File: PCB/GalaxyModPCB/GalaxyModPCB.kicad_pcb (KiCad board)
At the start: 2 copper layers, 63.5 x 38.2 mm, 65 parts, among them J1 LED RGBW Connector, J2 USB to UART, J3 Motor Connector, J4 Projector Connector, J5 Debug Header, J6 Power Header, J7 Boot mode, Q1 IRLML0030, Q2 IRLML0030, Q3 IRLML0030, Q4 IRLML0030, Q5 IRLML0030, Q6 IRLML0030, SW1 On/Off, SW2 Colour, SW3 Brightness, SW4 Motor, U1 ESP32-WROOM-32, U2 AMS1117-3.3

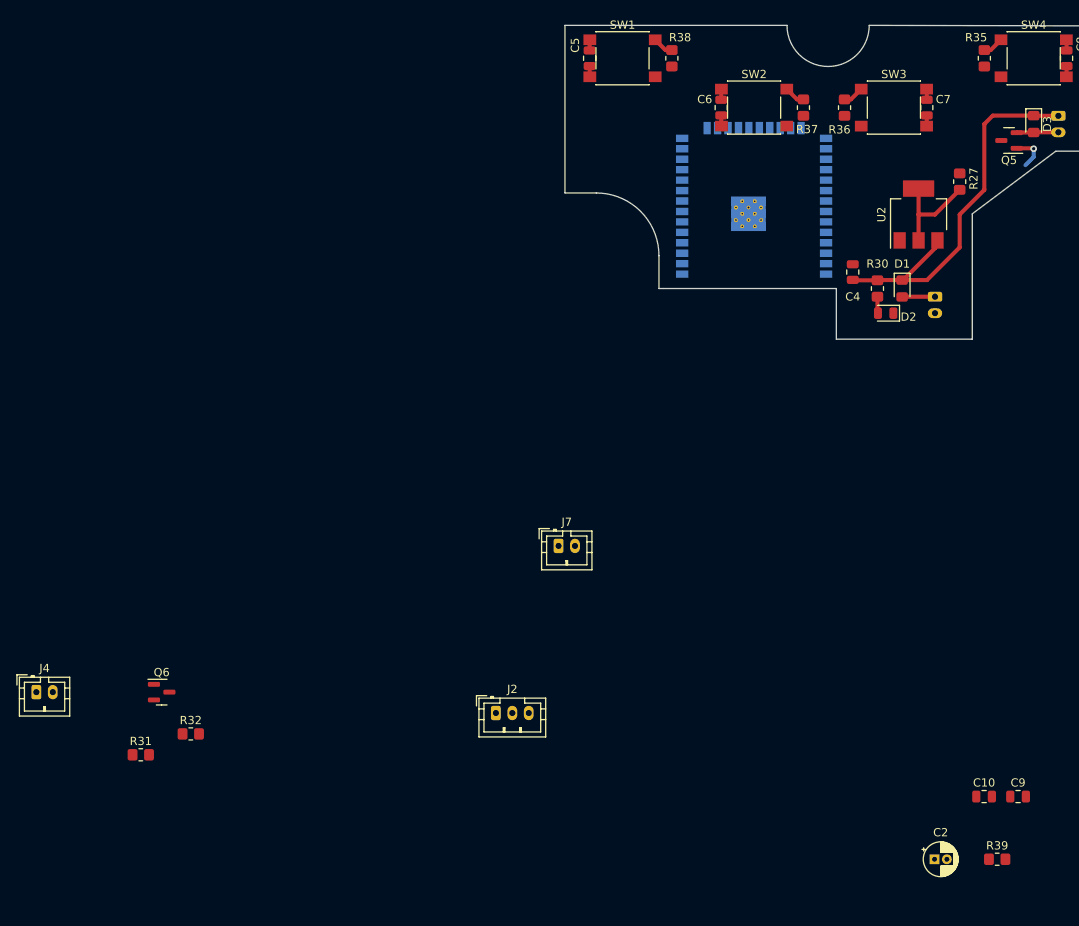
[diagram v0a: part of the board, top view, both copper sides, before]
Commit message: Connected power to esp32
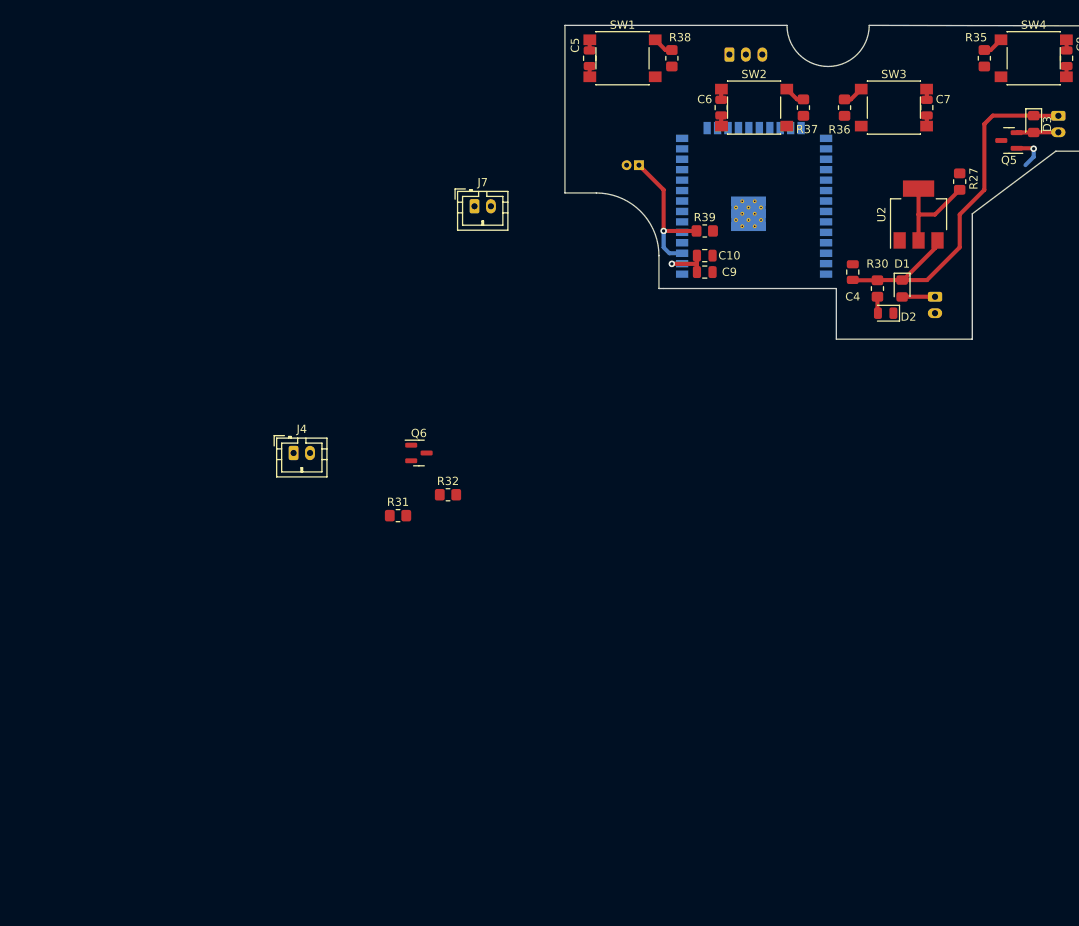
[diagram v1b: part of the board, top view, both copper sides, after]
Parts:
- C2, J2: moved to B.Cu
- moved C2 91.7 mm to (119.0, 68.0), turned to 180 degrees
- moved J2 85.0 mm to (130.0, 54.5)
- moved R39 84.3 mm to (127.0, 76.0)
- moved C9 74.3 mm to (127.0, 81.0)
- moved C10 74.0 mm to (127.0, 79.0)
- moved J4 42.7 mm to (77.0, 103.0)
- moved Q6 42.7 mm to (92.2, 103.0)
- moved R32 42.7 mm to (95.8, 108.1)
- moved R31 42.7 mm to (89.7, 110.6)
- moved J7 42.5 mm to (99.0, 73.0)
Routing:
- net Net-(C2-Pad1): track 0.00 -> 17.8 mm, vias 0 -> 1
- net Net-(C10-Pad1): track 3.93 -> 10.3 mm, vias 0 -> 1

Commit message: Traces
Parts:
- J4, R33, R34: moved to B.Cu
- moved J4 49.5 mm to (113.0, 69.0), turned to 90 degrees
- moved R33 42.7 mm to (165.0, 66.0), turned to 180 degrees
- moved R34 39.3 mm to (162.0, 63.0), turned to -90 degrees
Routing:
- net Net-(C10-Pad1): track 10.3 -> 112.9 mm
- net Net-(J5-Pad7): track 0.00 -> 3.41 mm
- net Net-(Q5-Pad1): track 4.50 -> 3.08 mm

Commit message: Fixed SW1 connection
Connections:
- C5 pad 2: +3.3V -> Net-(C10-Pad1)
- SW1 pad 2: +3.3V -> Net-(C10-Pad1)
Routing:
- net +3.3V: track 1.31 -> 0.00 mm
- net Net-(C10-Pad1): track 112.9 -> 114.2 mm

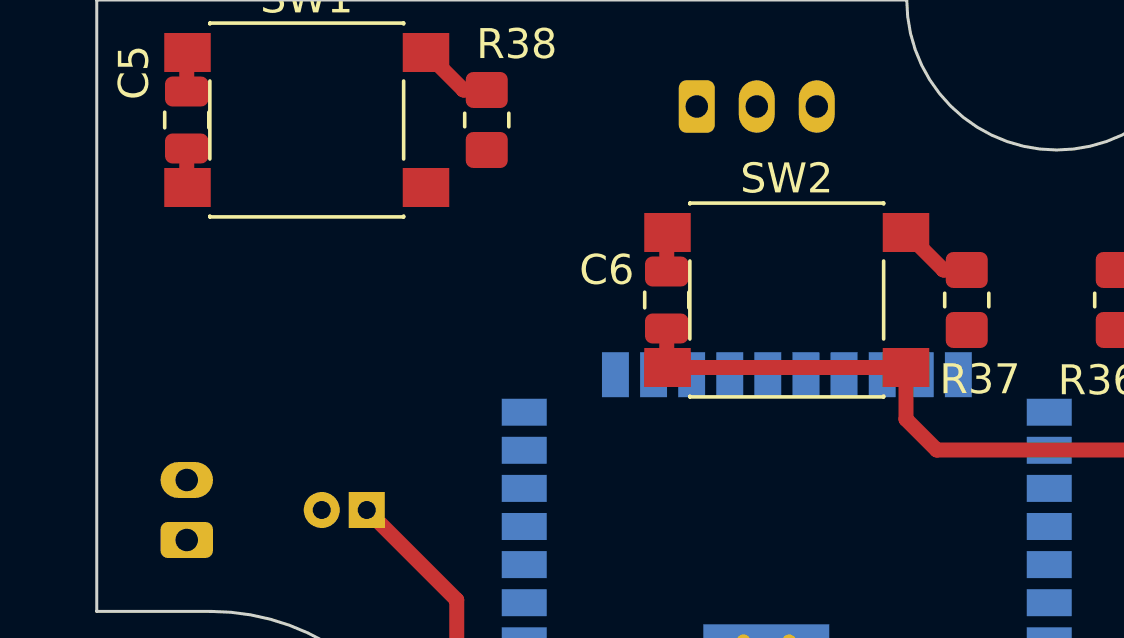
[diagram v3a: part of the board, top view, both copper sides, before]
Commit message: Powered switches
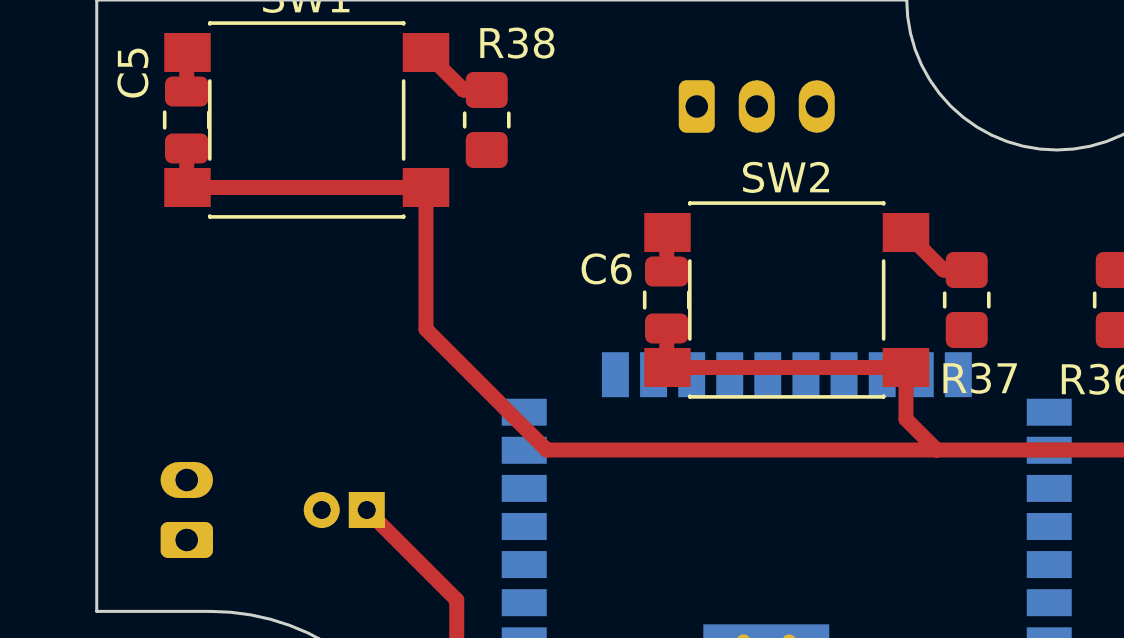
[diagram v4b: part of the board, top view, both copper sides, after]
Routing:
- net Net-(C10-Pad1): track 114.2 -> 145.6 mm
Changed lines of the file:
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@@
   (segment (start 146.025 65.025) (end 147 66) (width 0.5) (layer "F.Cu") (net 7))
   (segment (start 126.05 79.185051) (end 126.05 81) (width 0.5) (layer "F.Cu") (net 7))
+  (segment (start 125 66) (end 138 66) (width 0.5) (layer "F.Cu") (net 7))
   (segment (start 113 55.95) (end 113 57.225) (width 0.5) (layer "F.Cu") (net 7))
   (segment (start 138 66) (end 136.975 64.975) (width 0.5) (layer "F.Cu") (net 7))
+  (segment (start 120.975 61.975) (end 125 66) (width 0.5) (layer "F.Cu") (net 7))
   (segment (start 158 69) (end 151.05 69) (width 0.5) (layer "F.Cu") (net 7))
   (segment (start 155 66) (end 155 65.275) (width 0.5) (layer "F.Cu") (net 7))
@@
   (segment (start 158 69) (end 155 66) (width 0.5) (layer "F.Cu") (net 7))
   (segment (start 154 63.225) (end 153.975 63.25) (width 0.5) (layer "F.Cu") (net 7))
+  (segment (start 120.975 57.25) (end 120.975 61.975) (width 0.5) (layer "F.Cu") (net 7))
+  (segment (start 120.975 57.25) (end 113.025 57.25) (width 0.5) (layer "F.Cu") (net 7))
   (segment (start 126.05 79.95) (end 126.05 81) (width 0.5) (layer "F.Cu") (net 7))
   (via (at 123 80) (size 0.8) (drill 0.4) (layers "F.Cu" "B.Cu") (net 7))

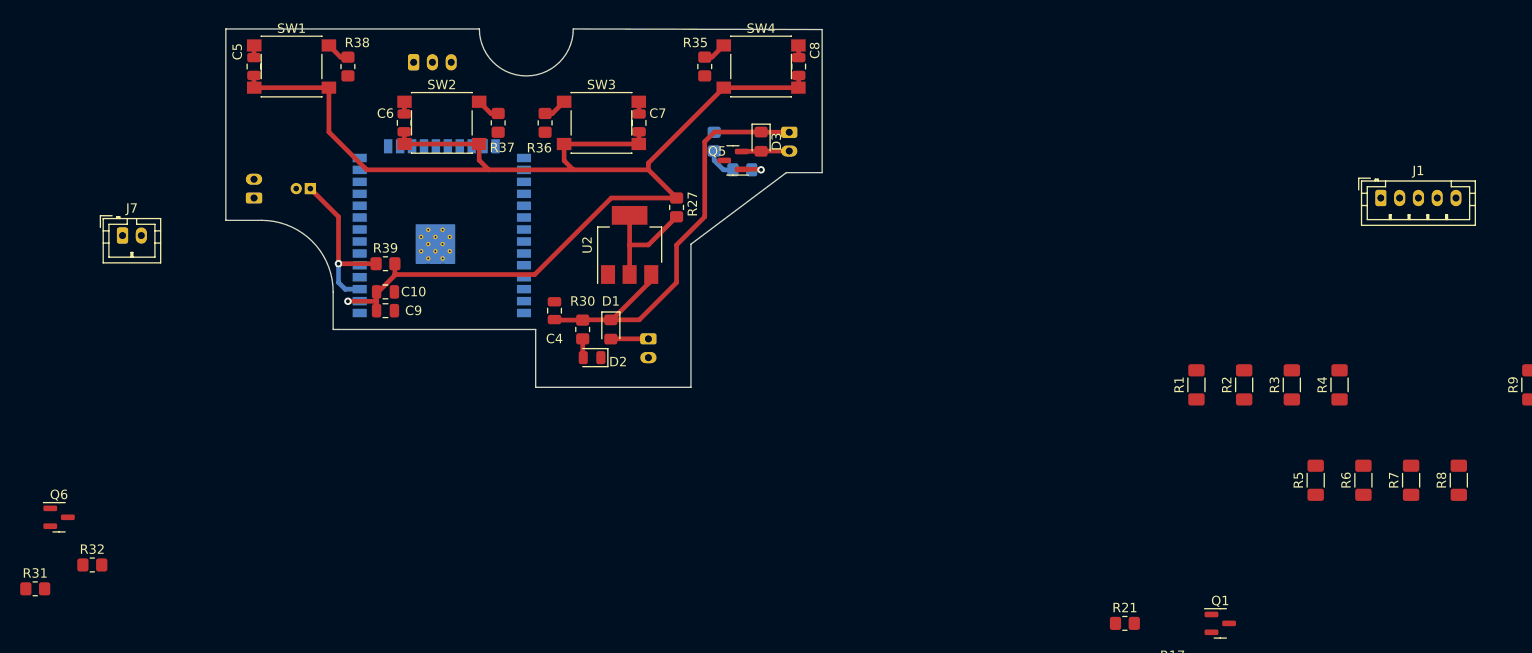
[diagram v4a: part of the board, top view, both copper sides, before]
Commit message: Wired up LED header
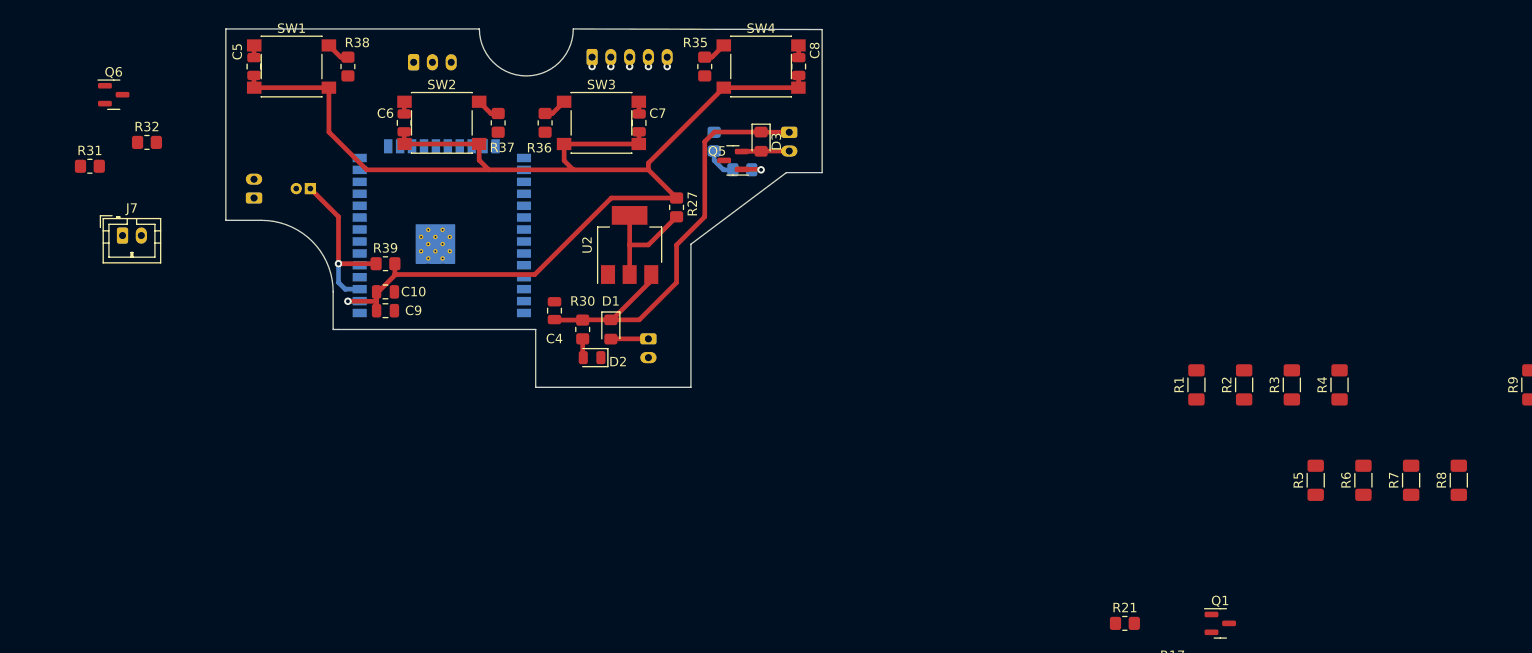
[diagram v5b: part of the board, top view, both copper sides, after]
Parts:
- J1: moved to B.Cu
- moved J1 85.3 mm to (149.0, 54.0)
- moved Q6 45.4 mm to (98.1, 58.0)
- moved R31 45.4 mm to (95.5, 65.6)
- moved R32 45.4 mm to (101.6, 63.1)
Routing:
- net Net-(J1-Pad5): track 0.00 -> 1.00 mm, vias 0 -> 1
- net Net-(J1-Pad4): track 0.00 -> 1.00 mm, vias 0 -> 1
- net Net-(J1-Pad3): track 0.00 -> 1.00 mm, vias 0 -> 1
- net Net-(J1-Pad2): track 0.00 -> 1.00 mm, vias 0 -> 1
- net Net-(D3-Pad1): track 46.2 -> 47.2 mm, vias 0 -> 1

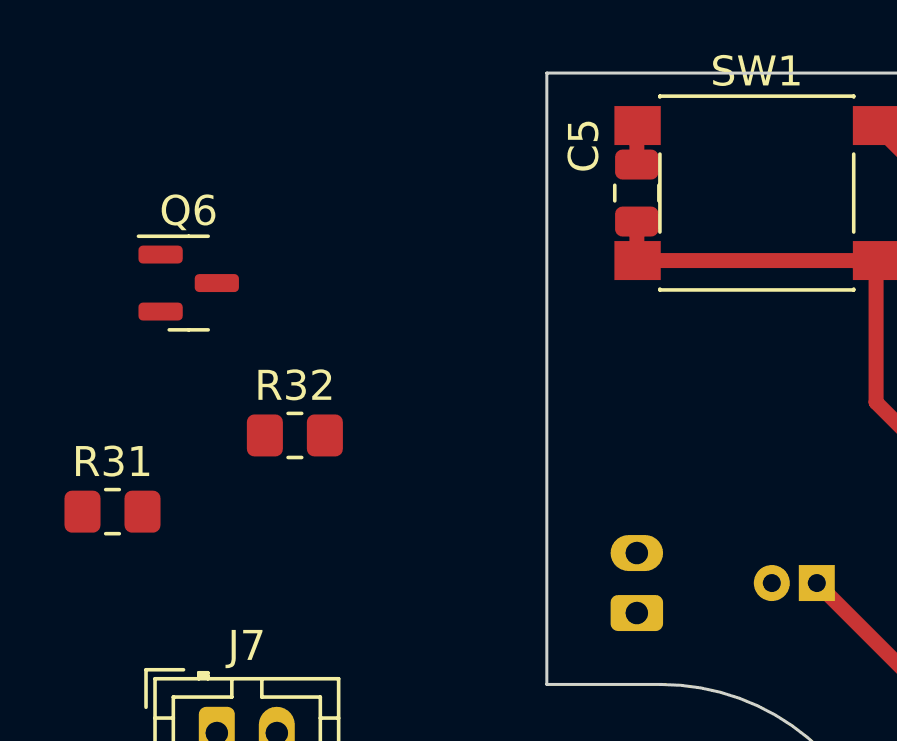
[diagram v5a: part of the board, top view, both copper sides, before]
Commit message: Began work on projector LED
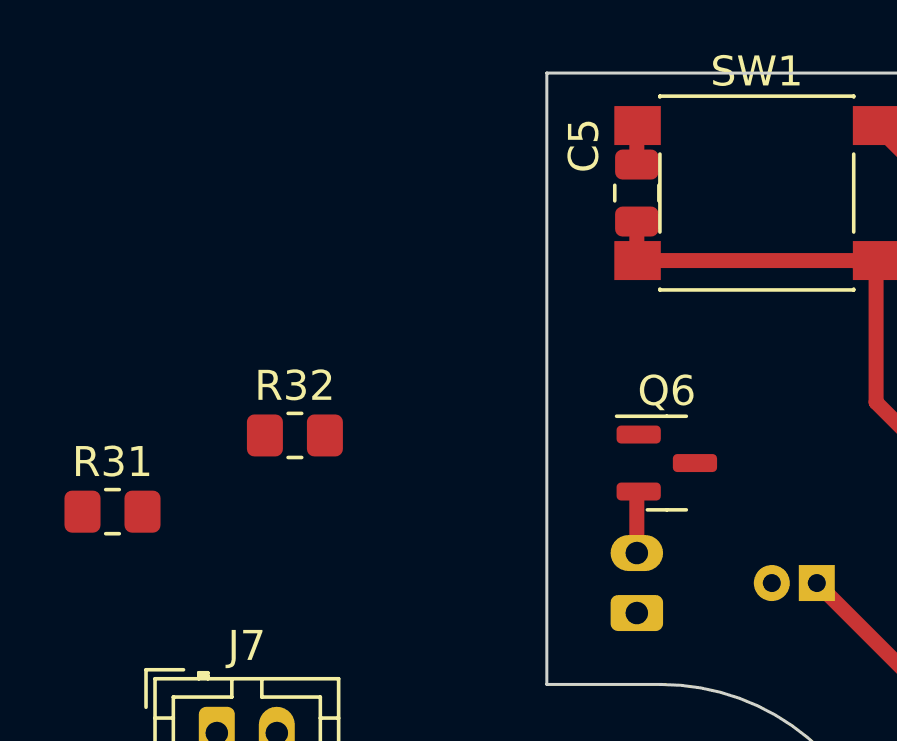
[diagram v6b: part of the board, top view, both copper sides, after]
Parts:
- moved Q6 17.0 mm to (114.0, 64.0)
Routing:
- net Net-(J4-Pad2): track 0.00 -> 2.08 mm
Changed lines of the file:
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@@
   )
   (footprint "Package_TO_SOT_SMD:SOT-23" (layer "F.Cu")
-    (at 98.0625 58)
+    (at 114 64)
     (descr "SOT, 3 Pin (https://www.jedec.org/system/files/docs/to-236h.pdf variant AB), generated with kicad-footprint-generator ipc_gullwing_generator.py")
     (tags "SOT TO_SOT_SMD")
@@
   (segment (start 157 54) (end 157 55) (width 0.5) (layer "F.Cu") (net 12))
   (via (at 157 55) (size 0.8) (drill 0.4) (layers "F.Cu" "B.Cu") (net 12))
+  (segment (start 113 65.0125) (end 113.0625 64.95) (width 0.5) (layer "F.Cu") (net 15))
+  (segment (start 113 67) (end 113 65.0125) (width 0.5) (layer "F.Cu") (net 15))
   (segment (start 162 65) (end 163 66) (width 0.5) (layer "B.Cu") (net 17))
   (segment (start 162 64) (end 162 65) (width 0.5) (layer "B.Cu") (net 17))

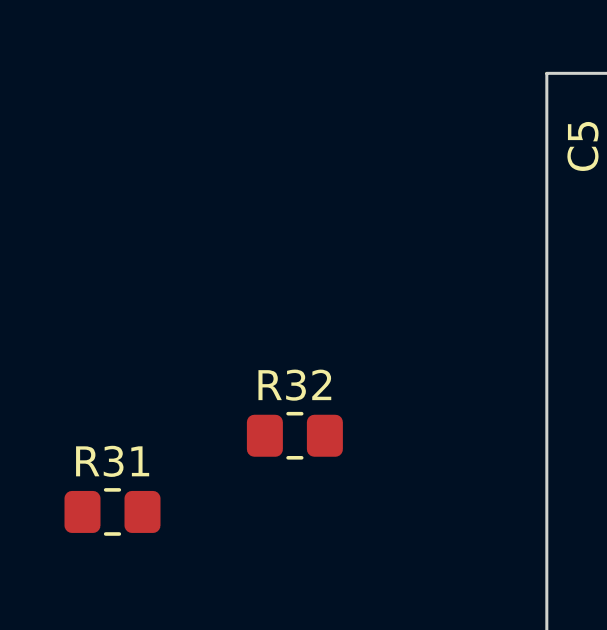
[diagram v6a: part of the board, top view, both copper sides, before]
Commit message: Updated projector LED requirements
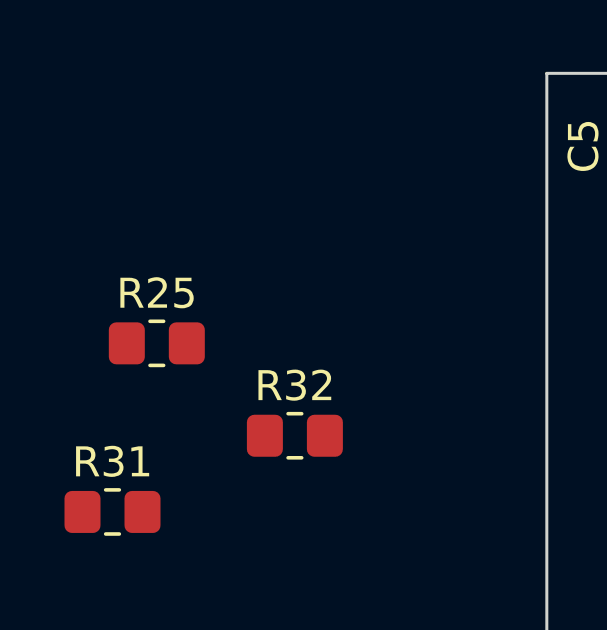
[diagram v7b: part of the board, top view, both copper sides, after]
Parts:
- added R25: 100, Resistor_SMD:R_0805_2012Metric_Pad1.20x1.40mm_HandSolder, F.Cu at (97.0, 60.0)
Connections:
- C4 pad 1: Net-(D3-Pad1) -> Net-(J4-Pad1)
- D1 pad 1: Net-(D3-Pad1) -> Net-(J4-Pad1)
- D3 pad 1: Net-(D3-Pad1) -> Net-(J4-Pad1)
- J1 pad 1: Net-(D3-Pad1) -> Net-(J4-Pad1)
- J3 pad 1: Net-(D3-Pad1) -> Net-(J4-Pad1)
- J4 pad 1: Net-(C10-Pad1) -> Net-(J4-Pad1)
- Q6 pad 2: Net-(J4-Pad2) -> Net-(Q6-Pad2)
- R30 pad 2: Net-(D3-Pad1) -> Net-(J4-Pad1)
- U2 pad 3: Net-(D3-Pad1) -> Net-(J4-Pad1)
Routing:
- net Net-(J4-Pad1): track 0.00 -> 47.2 mm, vias 0 -> 1
- net Net-(D3-Pad1): track 47.2 -> 0.00 mm, vias 1 -> 0
- net Net-(Q6-Pad2): track 0.00 -> 2.08 mm
- net Net-(J4-Pad2): track 2.08 -> 0.00 mm
